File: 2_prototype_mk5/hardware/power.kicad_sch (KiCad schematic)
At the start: 7 parts, among them J6 171825-4

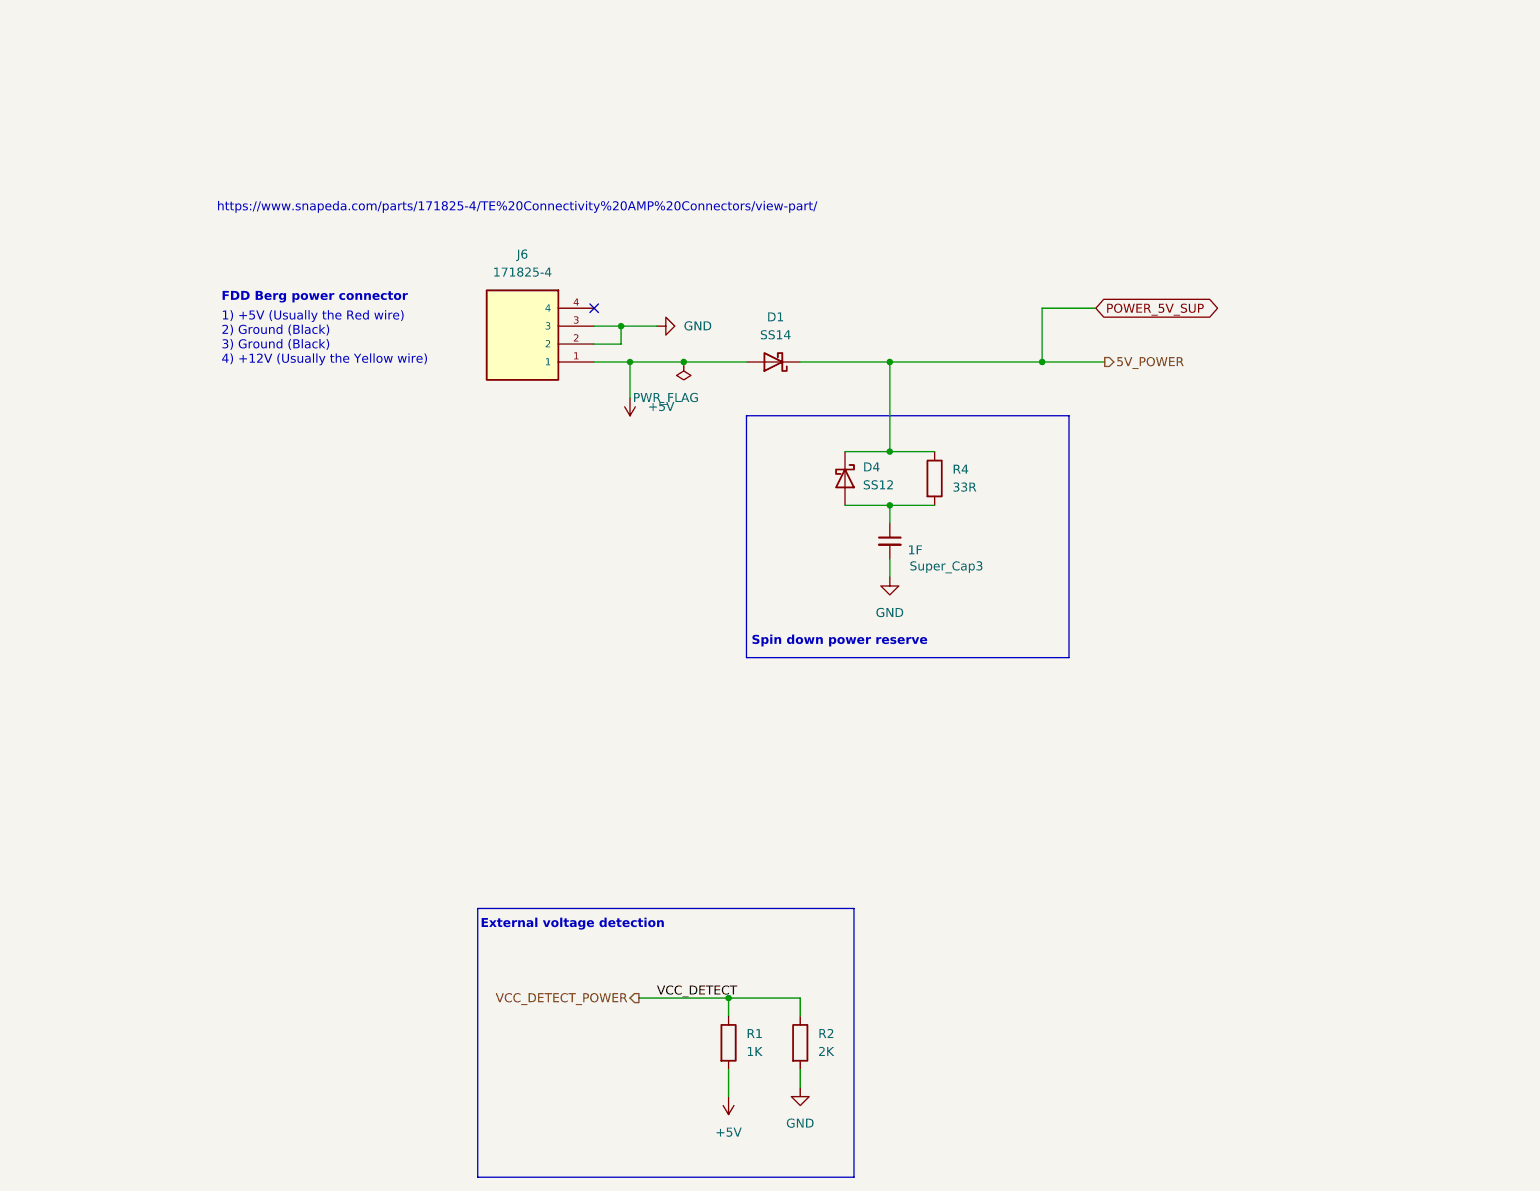
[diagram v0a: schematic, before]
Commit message: MKV - SATA connector and wiring complete
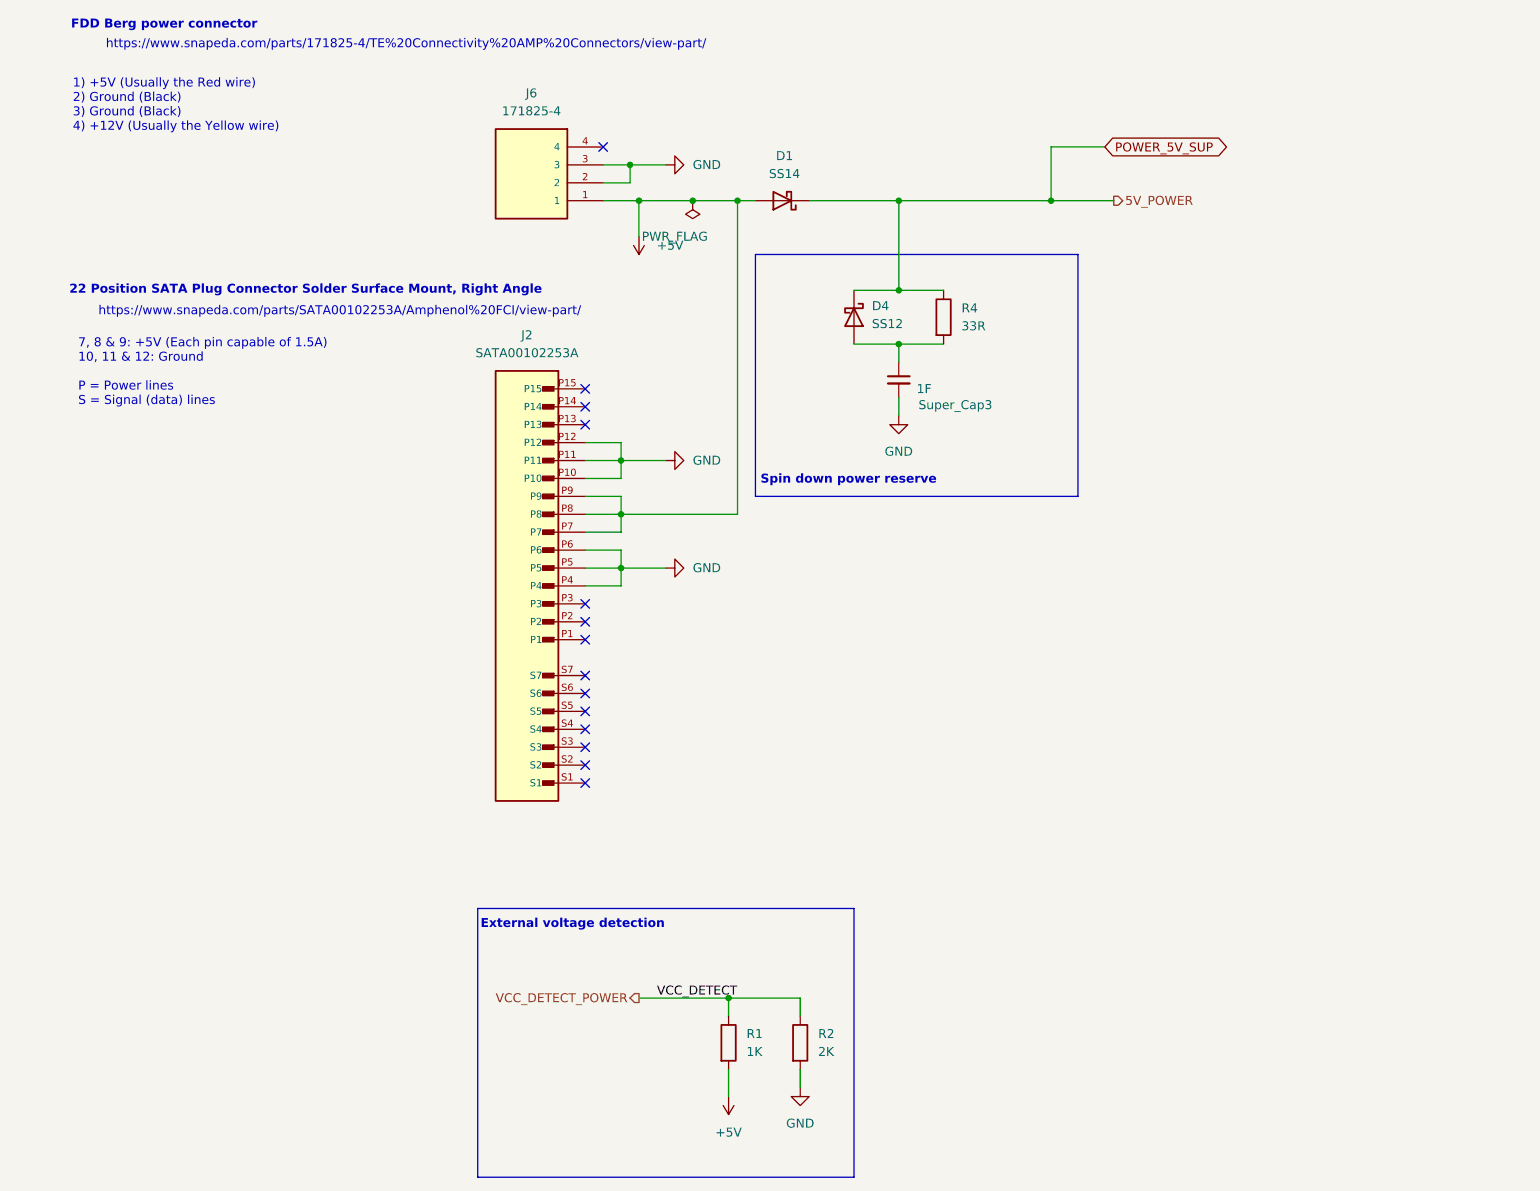
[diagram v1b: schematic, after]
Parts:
- added J2: SATA00102253A, Connector_SATA_SAS:SATA_Amphenol_10029364-001LF_Horizontal, symbol Project symbols:SATA00102253A
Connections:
- net +5V: now also J2.P7, J2.P8, J2.P9
- net GND: now also J2.P10, J2.P11, J2.P12, J2.P4, J2.P5, J2.P6
- no-connect marks 1 -> 14
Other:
- note added: "22 Position SATA Plug Connector Solder Surface Mount, Right Angle"
- note added: "7, 8 & 9: +5V (Each pin capable of 1.5A) 10, 11 & 12: Ground P = Power lines S = Signal (data) lines"
- note added: "https://www.snapeda.com/parts/SATA00102253A/Amphenol%20FCI/view-part/"
- moved on the sheet: D1, D4, J6, R4, Super_Cap3

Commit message: Major MKV redesign using embedded RP2350
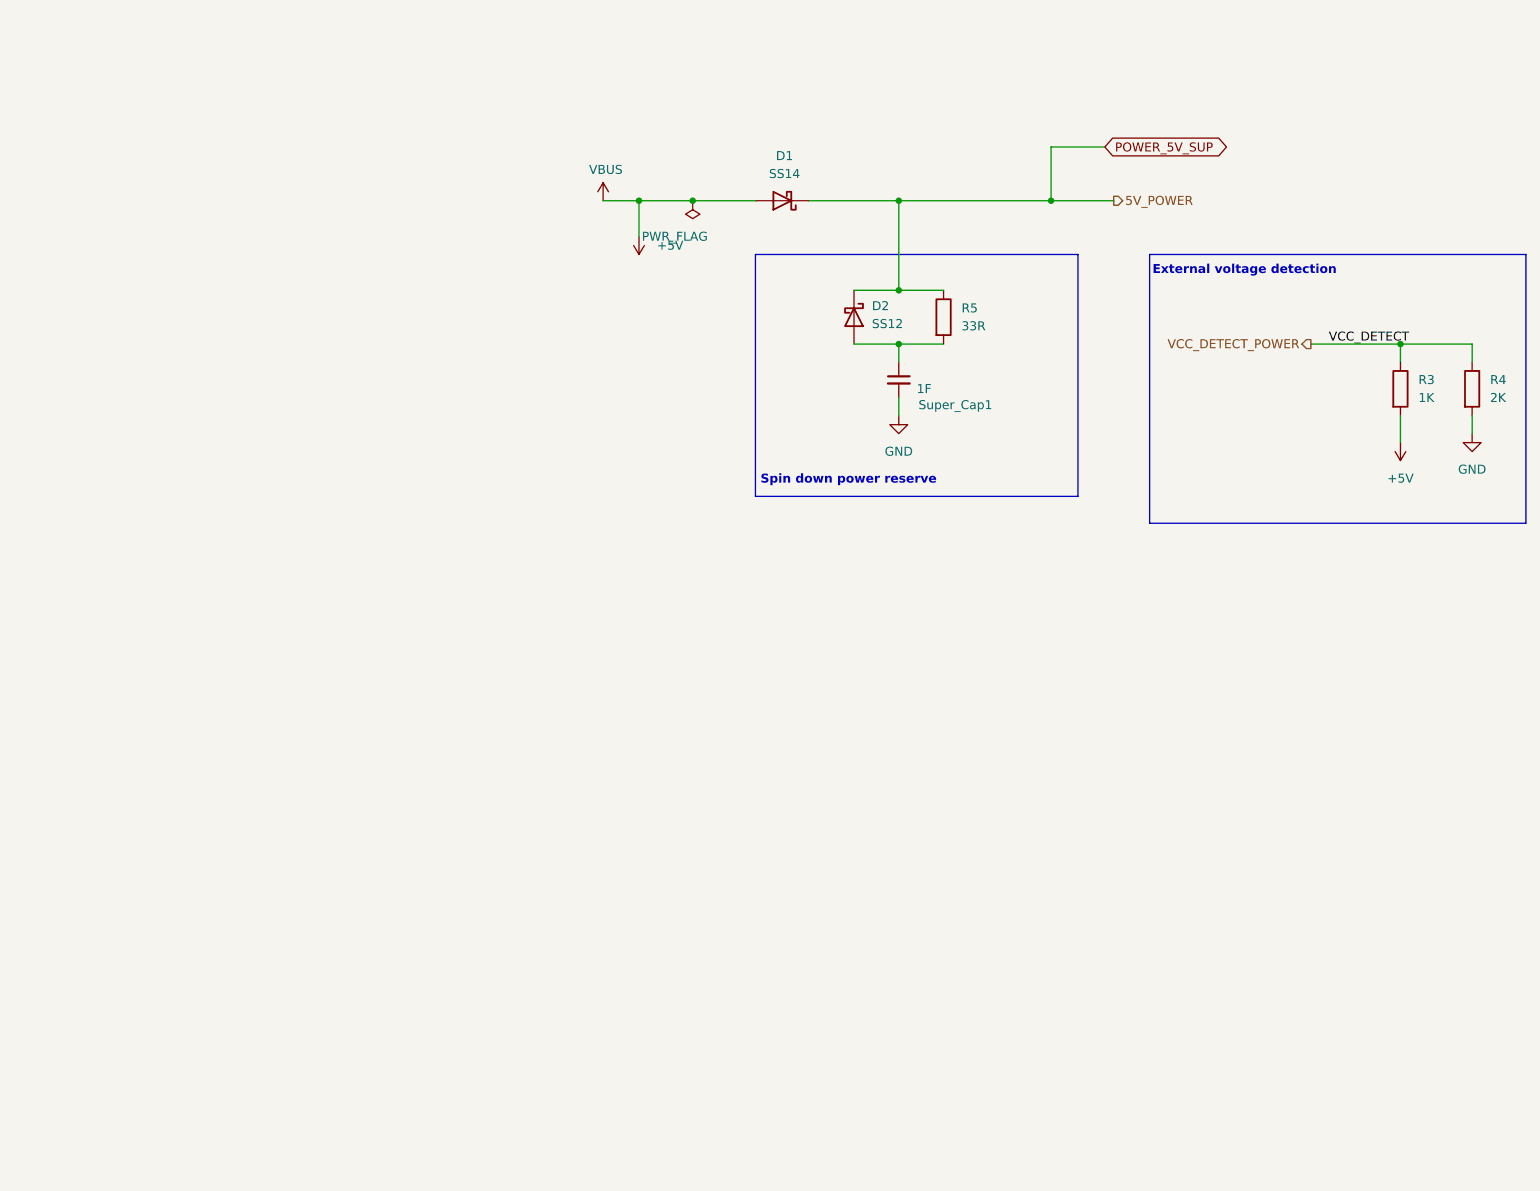
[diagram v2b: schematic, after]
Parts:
- removed J2: SATA00102253A, Connector_SATA_SAS:SATA_Amphenol_10029364-001LF_Horizontal, symbol Project symbols:SATA00102253A
- removed J6: 171825-4, Custom:TE_171825-4, symbol Project symbols:171825-4
- renumbered D4 to D2, R1 to R3, R2 to R4, R4 to R5, Super_Cap3 to Super_Cap1
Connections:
- no-connect marks 14 -> 0
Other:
- note removed: "1) +5V (Usually the Red wire) 2) Ground (Black) 3) Ground (Black) 4) +12V (Usually the Yellow wire)"
- note removed: "22 Position SATA Plug Connector Solder Surface Mount, Right Angle"
- note removed: "7, 8 & 9: +5V (Each pin capable of 1.5A) 10, 11 & 12: Ground P = Power lines S = Signal (data) lines"
- note removed: "FDD Berg power connector"
- note removed: "https://www.snapeda.com/parts/171825-4/TE%20Connectivity%20AMP%20Connectors/view-part/"
- note removed: "https://www.snapeda.com/parts/SATA00102253A/Amphenol%20FCI/view-part/"
- moved on the sheet: R3, R4

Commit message: MKV: Add LCSC numbers and resolve DRC errors
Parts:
- D1: LCSC_Part_Number (none) -> C2480
- D2: LCSC_Part_Number C184027 -> C2479
- R3: LCSC_Part_Number (none) -> C21190
- R4: LCSC_Part_Number (none) -> C4184
